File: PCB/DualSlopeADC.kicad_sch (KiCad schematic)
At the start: 18 parts, among them J1 RPi_GPIO, J5 Conn_01x02, J6 Conn_01x02, J7 Conn_01x02, Q1 PMOS, Q2 NMOS, Q4 PNP, U1 OPA1692xDGK, U2 OPA1692xDGK, U3 OPA1692xDGK

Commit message: .
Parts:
- removed C1: C, Capacitor_SMD:C_0805_2012Metric, symbol Device:C
- removed J1: RPi_GPIO, RPI_Hat:RPI_Hat_B+, symbol RPi_Hat:RPi_GPIO
- removed J5, J6, J7: Conn_01x02, Connector_PinHeader_2.54mm:PinHeader_1x02_P2.54mm_Vertical, symbol Connector_Generic:Conn_01x02
- removed Q1: PMOS, symbol Simulation_SPICE:PMOS
- removed Q2: NMOS, symbol Simulation_SPICE:NMOS
- removed Q4: PNP, symbol Simulation_SPICE:PNP
- removed R1, R2, R3, R4, R5, R6, R7: R, Resistor_SMD:R_0603_1608Metric, symbol Device:R
- removed U1, U2, U3: OPA1692xDGK, Package_SO:VSSOP-8_3x3mm_P0.65mm, symbol Amplifier_Operational:OPA1692xDGK
- added J1, J2: Conn_02x07_Counter_Clockwise, Connector_PinHeader_2.54mm:PinHeader_2x07_P2.54mm_Vertical, symbol Connector_Generic:Conn_02x07_Counter_Clockwise
- added U1: CH32V003FxPx, Package_SO:TSSOP-20_4.4x6.5mm_P0.65mm, symbol MCU_WCH_CH32V0:CH32V003FxPx
- added U2: ADR4533, Package_SO:SOIC-8_3.9x4.9mm_P1.27mm, symbol Reference_Voltage:ADR4533
- added U3: AD8606ARZ, Package_SO:SOIC-8_3.9x4.9mm_P1.27mm, symbol Amplifier_Operational:AD8606ARZ
- added U4: ADG419BRM, Package_SO:MSOP-8_3x3mm_P0.65mm, symbol Analog_Switch:ADG419BRM
- added U5: LTC6752xSC6-4, Package_TO_SOT_SMD:SOT-363_SC-70-6, symbol Comparator:LTC6752xSC6-4
- added U6: CA56-12EWA, Display_7Segment:CA56-12EWA, symbol Display_Character:CA56-12EWA
- added U8: 74HC595, Package_DIP:DIP-16_W7.62mm, symbol 74xx:74HC595

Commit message: PCB design anfang
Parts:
- removed J1, J2: Conn_02x07_Counter_Clockwise, Connector_PinHeader_2.54mm:PinHeader_2x07_P2.54mm_Vertical, symbol Connector_Generic:Conn_02x07_Counter_Clockwise
- removed U3: AD8606ARZ, Package_SO:SOIC-8_3.9x4.9mm_P1.27mm, symbol Amplifier_Operational:AD8606ARZ
- added C2, C3: 0.1u, Capacitor_SMD:C_0805_2012Metric, symbol Device:C
- added C4: 1m, Capacitor_SMD:C_0805_2012Metric, symbol Device:C
- added C5: 130p, Capacitor_SMD:C_0805_2012Metric, symbol Device:C
- added C6: 100u, Capacitor_THT:CP_Radial_D12.5mm_P5.00mm, symbol Device:C
- added J1, J3, J4, J5: Conn_01x02_Pin, Connector_PinHeader_2.54mm:PinHeader_1x02_P2.54mm_Vertical, symbol Connector:Conn_01x02_Pin
- added R1: 1k, Resistor_SMD:R_0603_1608Metric, symbol Device:R
- added R2: 10Meg, Resistor_SMD:R_0603_1608Metric, symbol Device:R
- added R3: 100k, Resistor_SMD:R_0603_1608Metric, symbol Device:R
- added U3: AD8605ARTZ-R2, footprints:SOT95P290X145-5N, symbol AD8605ARTZ-R2:AD8605ARTZ-R2
- added unit 2 of U4
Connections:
- net at U4.1: now also R3.1
- net at U4.2: now also C4.1, R1.2
- net GPIO_Control: now reaches U4.6
- net VCC_5V: now reaches U4.8
- net VCC_5V: now also U1.9 (VDD), U2.2 (IN), U5.5 (VDD), U5.6 (VCC), C2.1, C6.1, J3.1 (Pin_1), U3.5 (V+), U4.4 (V+), U4.5 (VL)
- net GPIO_Input: now reaches U5.1
- net GND: now reaches U5.2 (VEE)
- net GND: now also U1.7 (VSS), U2.4 (GND), C2.2, C3.2, C4.2, C6.2, J3.2 (Pin_2), J4.2 (Pin_2), J5.2 (Pin_2), U3.2 (V-), U4.3 (GND), U4.7 (V-)
- net VCC_3V3: now reaches U5.3 (+)
- net VCC_3V3: now also C3.1, J1.2 (Pin_2), J4.1 (Pin_1), R2.2, U3.3 (+INA)
- net at U5.4 (-): now also C5.2, U3.1 (OUTA)
- net RESET: now reaches U1.4 (PD7)
- net at U2.6 (OUT): now also J1.1 (Pin_1)
- new net: C5.1, R3.2, U3.4 (-INA)
- new net Vin: J5.1 (Pin_1), R1.1, R2.1
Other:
- moved on the sheet: U1, U2, U4A, U5, U6, U8

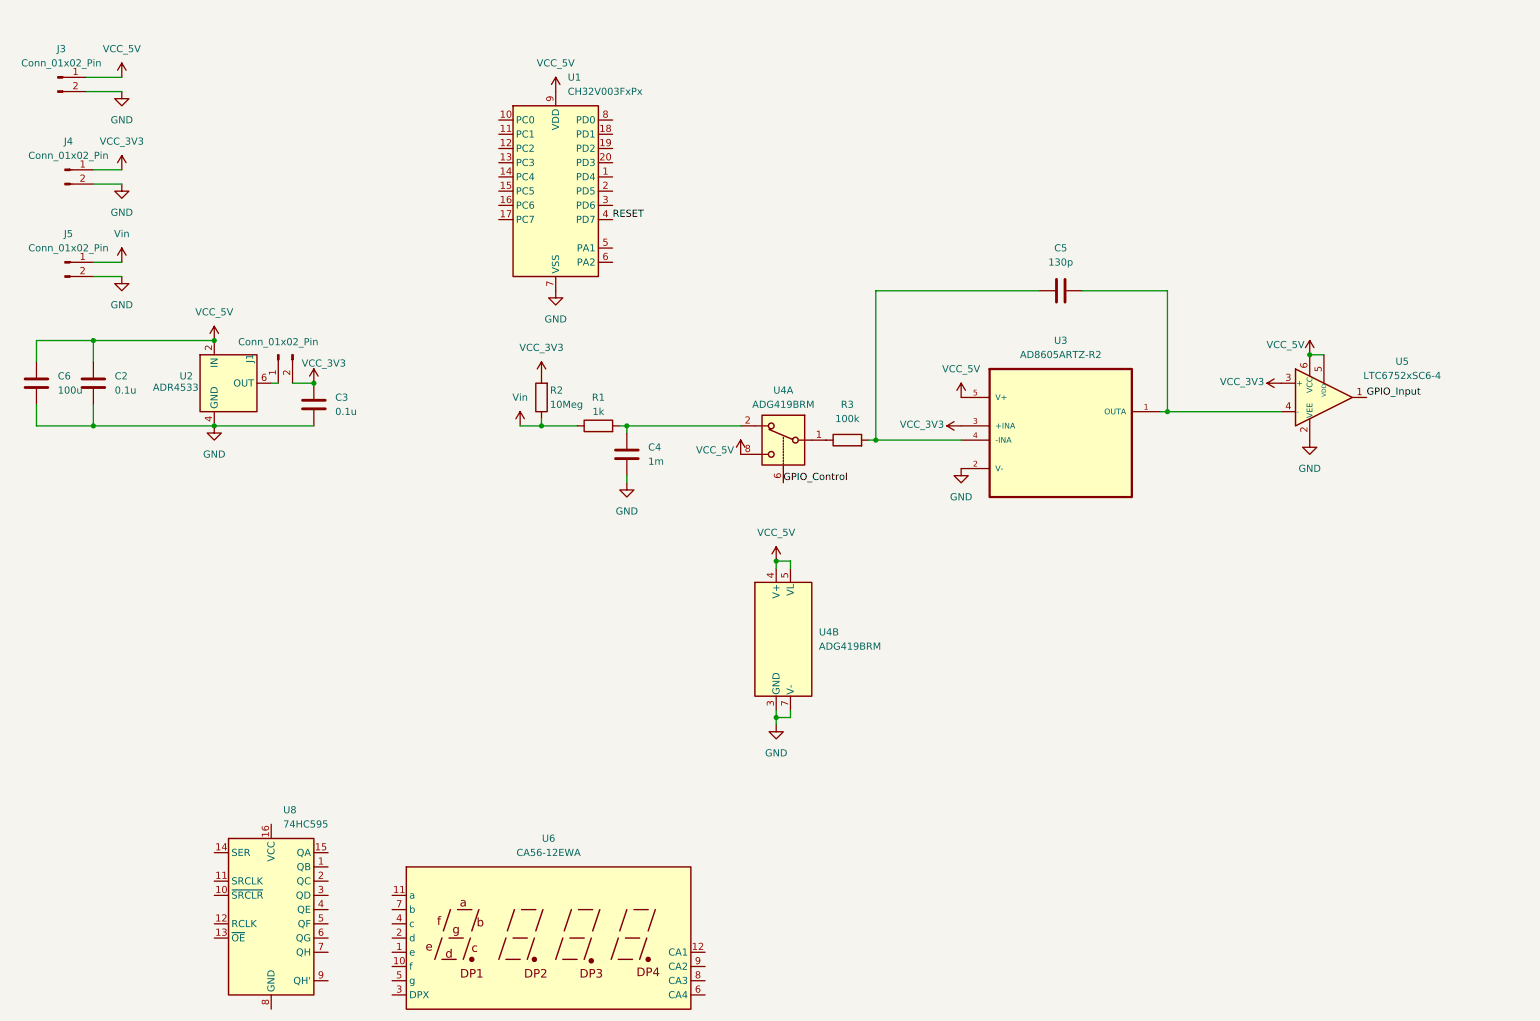
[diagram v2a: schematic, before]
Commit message: CH32fun integriert
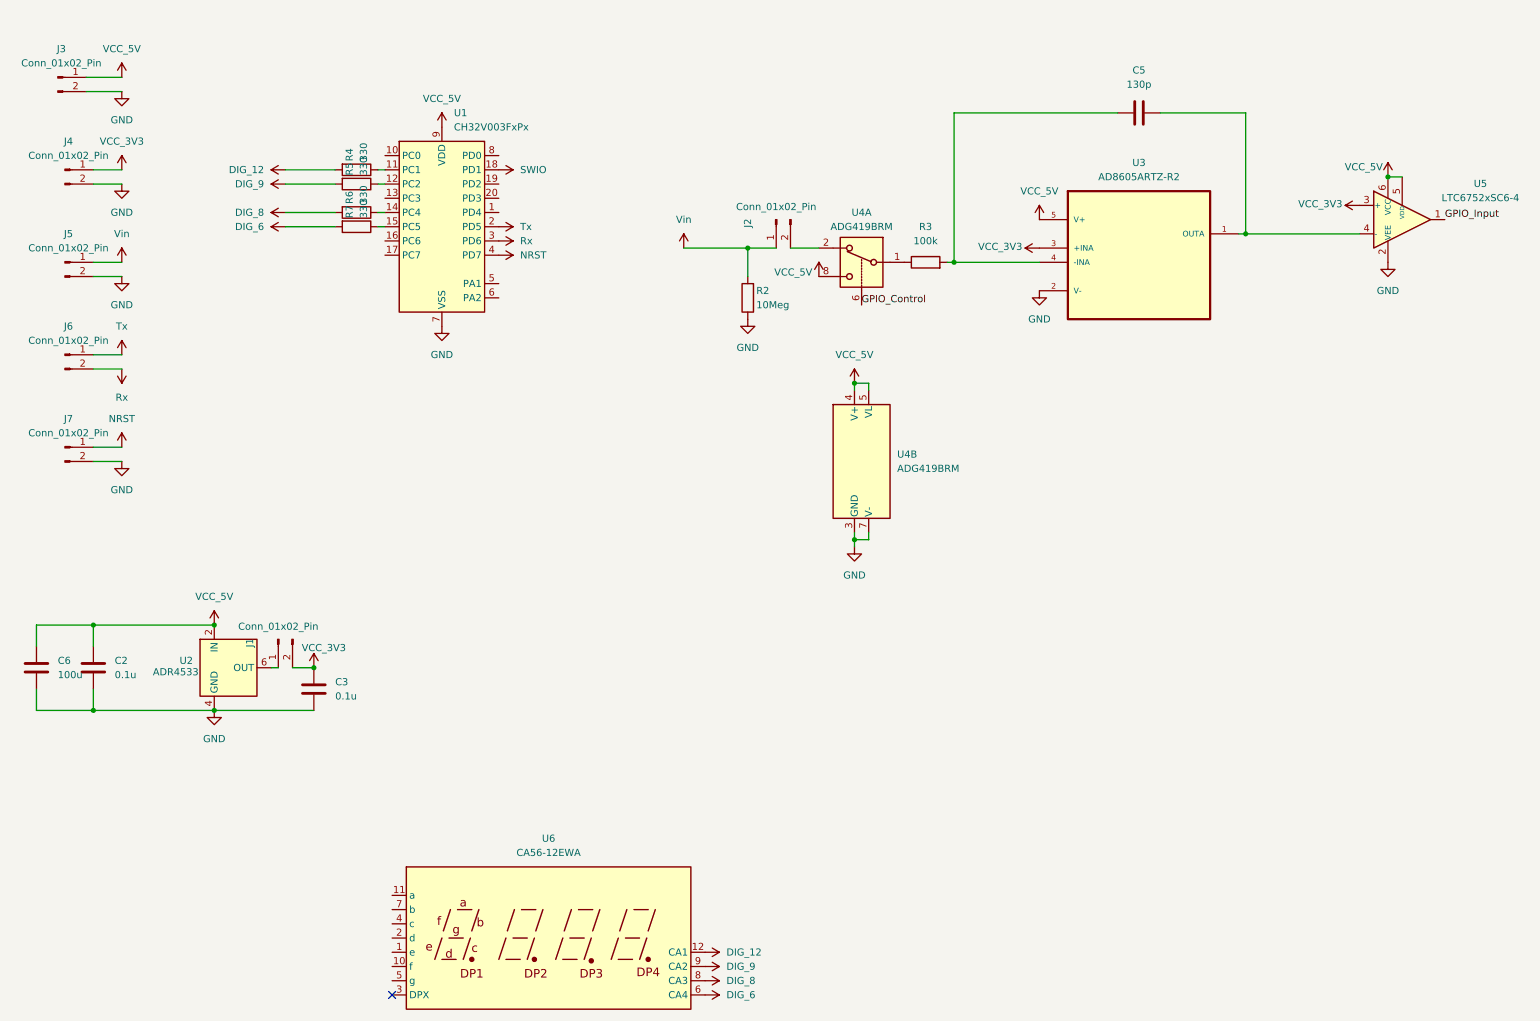
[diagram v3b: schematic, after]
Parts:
- removed C4: 1m, Capacitor_SMD:C_0805_2012Metric, symbol Device:C
- removed R1: 1k, Resistor_SMD:R_0603_1608Metric, symbol Device:R
- removed U8: 74HC595, Package_DIP:DIP-16_W7.62mm, symbol 74xx:74HC595
- added J2, J6, J7: Conn_01x02_Pin, Connector_PinHeader_2.54mm:PinHeader_1x02_P2.54mm_Vertical, symbol Connector:Conn_01x02_Pin
- added R4, R5, R6, R7: 330, Resistor_SMD:R_0603_1608Metric, symbol Device:R
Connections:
- net GND: now also R2.1, J7.2 (Pin_2)
- net VCC_3V3: no longer R2.2
- net Vin: now also R2.2, J2.1 (Pin_1); no longer R2.1
- net at U4.2: now also J2.2 (Pin_2)
- net DIG_12: now reaches U6.12 (CA1)
- net DIG_12: now also R4.2
- net DIG_6: now reaches U6.6 (CA4)
- net DIG_6: now also R7.2
- net DIG_8: now reaches U6.8 (CA3)
- net DIG_8: now also R6.2
- net DIG_9: now reaches U6.9 (CA2)
- net DIG_9: now also R5.2
- net at U1.11 (PC1): now also R4.1
- net at U1.12 (PC2): now also R5.1
- net at U1.14 (PC4): now also R6.1
- net at U1.15 (PC5): now also R7.1
- net SWIO: now reaches U1.18 (PD1)
- net Tx: now reaches U1.2 (PD5)
- net Tx: now also J6.1 (Pin_1)
- net Rx: now reaches U1.3 (PD6)
- net Rx: now also J6.2 (Pin_2)
- net RESET renamed NRST
- net NRST: now also J7.1 (Pin_1)
- no-connect marks 0 -> 1
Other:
- moved on the sheet: C2, C3, C5, C6, J1, R2, R3, U1, U2, U3, U4A, U4B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

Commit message: pcb weiter
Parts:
- added C4: 0.1u, Capacitor_SMD:C_0805_2012Metric, symbol Device:C
- U6: footprint Display_7Segment:CA56-12EWA -> 3461BS_4Digit_7SegDisplay:3461BS_4Digit_7SegDisplay
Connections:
- net GPIO_Control is gone; now on net ADC_Control: U4.6
- net GPIO_Input is gone; now on net COMP_OUT: U5.1
- net GND: now also C4.1
- net NRST: now also C4.2
- net at R4.1: now also U1.15 (PC5); no longer U1.11 (PC1)
- net at R7.1: now also U1.1 (PD4); no longer U1.15 (PC5)
- net at R6.1: now also U1.11 (PC1); no longer U1.14 (PC4)
- net DIG_E: now reaches U6.1 (e)
- net DIG_E: now also U1.16 (PC6)
- net DIG_F: now reaches U6.10 (f)
- net DIG_F: now also U1.13 (PC3)
- net DIG_A: now reaches U6.11 (a)
- net DIG_A: now also U1.14 (PC4)
- net DIG_D: now reaches U6.2 (d)
- net DIG_D: now also U1.17 (PC7)
- net DIG_C: now reaches U6.4 (c)
- net DIG_C: now also U1.19 (PD2)
- net DIG_G: now reaches U6.5 (g)
- net DIG_G: now also U1.20 (PD3)
- net DIG_B: now reaches U6.7 (b)
- net DIG_B: now also U1.10 (PC0)
- net COMP_OUT: now reaches U1.5 (PA1)
- net COMP_OUT: now also U1.6 (PA2)
- net ADC_Control: now reaches U1.8 (PD0)

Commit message: Software inm Mounriver studio
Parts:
- added J8: Conn_01x02_Pin, Connector_PinHeader_2.54mm:PinHeader_1x02_P2.54mm_Vertical, symbol Connector:Conn_01x02_Pin
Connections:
- net COMP_OUT: no longer U1.6 (PA2)
- net Vin: now also J8.1 (Pin_1)
- new net: J8.2 (Pin_2), U1.6 (PA2)
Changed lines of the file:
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@@
 	)
 	(junction
-		(at 48.26 116.84)
+		(at 138.43 49.53)
 		(diameter 0)
 		(color 0 0 0 0)
 	)
 	(junction
-		(at 143.51 49.53)
+		(at 48.26 116.84)
 		(diameter 0)
 		(color 0 0 0 0)
 	)
 	(junction
-		(at 31.75 85.09)
+		(at 143.51 49.53)
 		(diameter 0)
 		(color 0 0 0 0)
 	)
 	(junction
-		(at 257.81 36.83)
+		(at 31.75 85.09)
 		(diameter 0)
 		(color 0 0 0 0)
 	)
 	(junction
-		(at 100.33 57.15)
+		(at 257.81 36.83)
 		(diameter 0)
 		(color 0 0 0 0)
@@
 	(wire
 		(pts
-			(xy 100.33 57.15) (xy 100.33 58.42)
+			(xy 129.54 58.42) (xy 138.43 58.42)
 		)
 		(stroke
@@
 	(wire
 		(pts
-			(xy 132.08 49.53) (xy 143.51 49.53)
+			(xy 132.08 49.53) (xy 138.43 49.53)
+		)
+		(stroke
+			(width 0)
+			(type default)
+		)
+	)
+	(wire
+		(pts
+			(xy 138.43 49.53) (xy 143.51 49.53)
 		)
 		(stroke
@@
 	(wire
 		(pts
-			(xy 99.06 55.88) (xy 100.33 55.88)
+			(xy 99.06 55.88) (xy 102.87 55.88)
 		)
 		(stroke
@@
 	(wire
 		(pts
-			(xy 100.33 57.15) (xy 100.33 55.88)
-		)
-		(stroke
-			(width 0)
-			(type default)
-		)
-	)
-	(wire
-		(pts
 			(xy 162.56 73.66) (xy 165.1 73.66)
 		)
@@
 	(wire
 		(pts
-			(xy 232.41 46.99) (xy 231.14 46.99)
+			(xy 99.06 58.42) (xy 127 58.42)
 		)
 		(stroke
@@
 	(wire
 		(pts
-			(xy 62.23 124.46) (xy 66.04 124.46)
-		)
-		(stroke
-			(width 0)
-			(type default)
-		)
-	)
-	(wire
-		(pts
-			(xy 99.06 58.42) (xy 100.33 58.42)
+			(xy 232.41 46.99) (xy 231.14 46.99)
 		)
 		(stroke
@@
 	(wire
 		(pts
-			(xy 102.87 57.15) (xy 100.33 57.15)
+			(xy 62.23 124.46) (xy 66.04 124.46)
 		)
 		(stroke
@@
 	(wire
 		(pts
+			(xy 138.43 58.42) (xy 138.43 49.53)
+		)
+		(stroke
+			(width 0)
+			(type default)
+		)
+	)
+	(wire
+		(pts
 			(xy 26.67 35.56) (xy 31.75 35.56)
 		)
@@
 	)
 	(symbol
+		(lib_id "Connector:Conn_01x02_Pin")
+		(at 129.54 63.5 270)
+		(mirror x)
+		(unit 1)
+		(exclude_from_sim no)
+		(in_bom yes)
+		(on_board yes)
+		(dnp no)
+		(property "Reference" "J8"
+			(at 134.62 62.865 0)
+			(effects
+				(font
+					(size 1.27 1.27)
+				)
+			)
+		)
+		(property "Value" "Conn_01x02_Pin"
+			(at 129.54 65.786 90)
+			(effects
+				(font
+					(size 1.27 1.27)
+				)
+			)
+		)
+		(property "Footprint" "Connector_PinHeader_2.54mm:PinHeader_1x02_P2.54mm_Vertical"
+			(at 129.54 63.5 0)
+			(effects
+				(font
+					(size 1.27 1.27)
+				)
+				(hide yes)
+			)
+		)
+		(property "Datasheet" "~"
+			(at 129.54 63.5 0)
+			(effects
+				(font
+					(size 1.27 1.27)
+				)
+				(hide yes)
+			)
+		)
+		(property "Description" "Generic connector, single row, 01x02, script generated"
+			(at 129.54 63.5 0)
+			(effects
+				(font
+					(size 1.27 1.27)
+				)
+				(hide yes)
+			)
+		)
+		(pin "2"
+		)
+		(pin "1"
+		)
+		(instances
+			(project "DualSlopeADC"
+				(path "/283011ff-11cf-4a24-84b5-14acf4ed13a0"
+					(reference "J8")
+					(unit 1)
+				)
+			)
+		)
+	)
+	(symbol
 		(lib_id "power:VCC")
 		(at 80.01 172.72 90)
@@
 	(symbol
 		(lib_id "power:VCC")
-		(at 102.87 57.15 0)
+		(at 102.87 55.88 270)
 		(unit 1)
 		(exclude_from_sim no)
@@
 		(dnp no)
 		(property "Reference" "#PWR054"
-			(at 102.87 60.96 0)
+			(at 99.06 55.88 0)
 			(effects
 				(font
@@
 		)
 		(property "Value" "COMP_OUT"
-			(at 108.966 57.404 0)
+			(at 111.252 56.134 90)
 			(effects
 				(font
@@
 		)
 		(property "Footprint" ""
-			(at 102.87 57.15 0)
+			(at 102.87 55.88 0)
 			(effects
 				(font
@@
 		)
 		(property "Datasheet" ""
-			(at 102.87 57.15 0)
+			(at 102.87 55.88 0)
 			(effects
 				(font
@@
 		)
 		(property "Description" "Power symbol creates a global label with name \"VCC\""
-			(at 102.87 57.15 0)
+			(at 102.87 55.88 0)
 			(effects
 				(font

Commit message: platine fertig
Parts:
- removed J1, J4: Conn_01x02_Pin, Connector_PinHeader_2.54mm:PinHeader_1x02_P2.54mm_Vertical, symbol Connector:Conn_01x02_Pin
- added J9: Conn_01x02_Pin, Connector_PinHeader_2.54mm:PinHeader_1x02_P2.54mm_Vertical, symbol Connector:Conn_01x02_Pin
- added U7: AD8656, Package_SO:SOIC-8_3.9x4.9mm_P1.27mm, symbol Amplifier_Operational:AD8656
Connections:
- net GND: now also U7.4 (V-)
- net SWIO: now also J9.1 (Pin_1)
- net VCC_3V3: now also U2.6 (OUT), J9.2 (Pin_2)
- net VCC_5V: now also U7.8 (V+)
- net Vin: now also U7.2 (-); no longer J2.1 (Pin_1), J8.1 (Pin_1), R2.2
- net ADC_IN_EXT: now reaches U4.2
- net ADC_IN_EXT: now also J8.2 (Pin_2), R2.2; no longer J2.2 (Pin_2)
- net ADC_IN_MC: now reaches U1.6 (PA2)
- net ADC_IN_MC: now also J2.2 (Pin_2); no longer J8.2 (Pin_2)
- new net: J2.1 (Pin_1), J8.1 (Pin_1), U7.1, U7.3 (+)
- no-connect marks 1 -> 4
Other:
- moved on the sheet: J2, J8, U4B
